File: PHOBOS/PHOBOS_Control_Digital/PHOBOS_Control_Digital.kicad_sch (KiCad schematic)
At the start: 79 parts, among them J1 Conn_01x06, J12 PWR, J14 PS1-2, J15 PS3-4, J2 RF_OUT, J3 USB4056-03-A_REVA2, J4 Screw_Terminal_01x02, J8 Conn_01x02, SW1 KMR211GLFS, U1 SX1280IMLTRT, U2 W25Q128JVSIQ, U3 NCP1117-3.3_SOT223, U4 RP2040, U5 TPS60403DBV, Y1 C1E-52.000-10-1012-X-M, Y2 ABM8-272-T3

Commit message: Schematic cleaned up for review.
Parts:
- removed J1: Conn_01x06, Connector_PinHeader_2.54mm:PinHeader_1x06_P2.54mm_Vertical, symbol Connector_Generic:Conn_01x06
- removed R2: 10k, Resistor_SMD:R_0402_1005Metric, symbol Device:R
- removed SW1: KMR211GLFS, External/Custom Parts:KMR2xxG_CNK, symbol KMR2xxG_CNK:KMR211GLFS
- removed TP12: GPIO22, TestPoint:TestPoint_THTPad_D2.0mm_Drill1.0mm, symbol Connector:TestPoint
- removed TP3: SCK_TRANS, TestPoint:TestPoint_Plated_Hole_D2.0mm, symbol Connector:TestPoint
- removed TP4: MOSI_TRANS, TestPoint:TestPoint_Plated_Hole_D2.0mm, symbol Connector:TestPoint
- removed TP5: MISO_TRANS, TestPoint:TestPoint_Plated_Hole_D2.0mm, symbol Connector:TestPoint
- removed TP6: CS, TestPoint:TestPoint_Plated_Hole_D2.0mm, symbol Connector:TestPoint
- J8: value Conn_01x02 -> BOOT; now left out of the parts list
- TP11: value GPIO22 -> GPIO19
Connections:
- net RUN: no longer names the net of U4.26 (RUN)
- no-connect marks 22 -> 25
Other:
- note added: "-3V Charge Pump"
- note added: "Connectors"
- note added: "Transceiver"
- note removed: "Boot Select"
- note removed: "Exclude From Board"
- note removed: "Filtering"
- note removed: "Make sure C10 is close to pin 44 of RP2040 ***C10 is out of date. figure out***"
- note removed: "Make sure R3 and R4 are close to RP2040"
- note removed: "Reset"
- note removed: "SPI1"
- moved on the sheet: C0, C1, C10, C11, C12, C13, C14, C15, C16, C17, C2, C3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

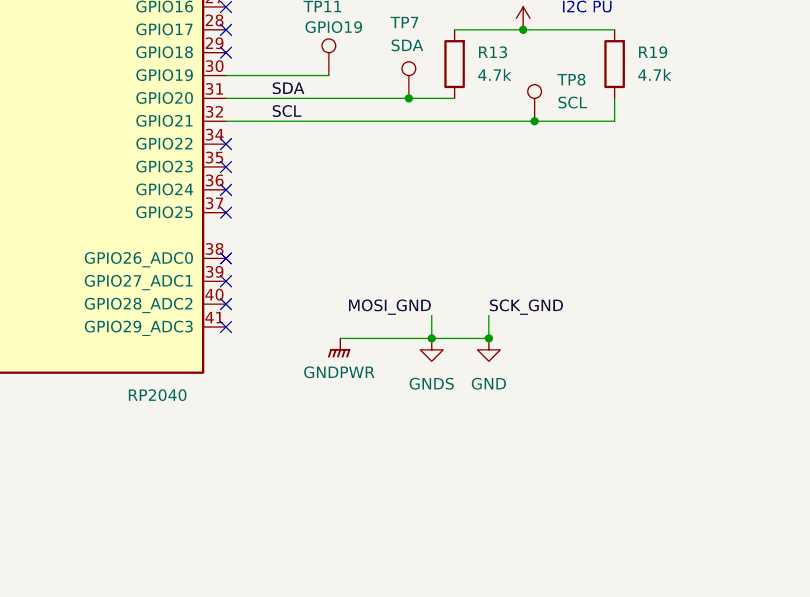
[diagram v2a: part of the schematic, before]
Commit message: Batt measure added
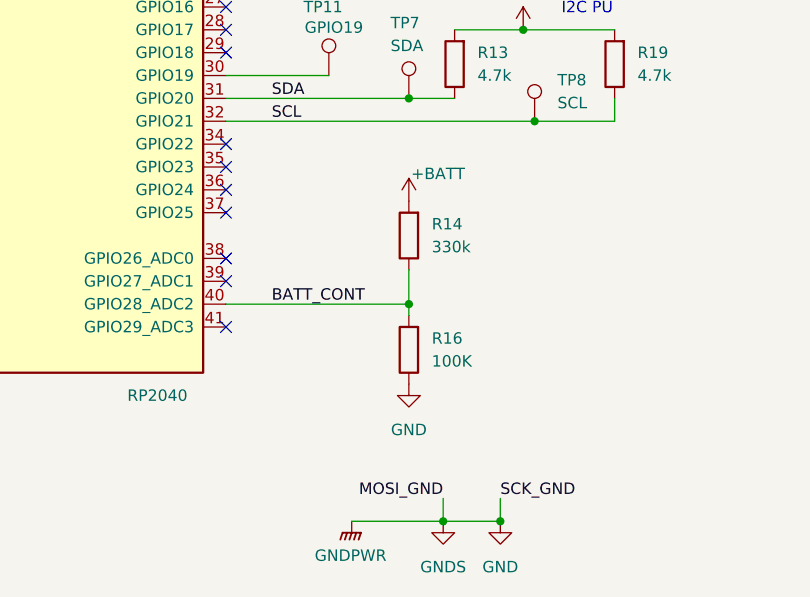
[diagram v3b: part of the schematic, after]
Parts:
- added R14: 330k, Resistor_SMD:R_0402_1005Metric, symbol Device:R
- added R16: 100K, Resistor_SMD:R_0402_1005Metric, symbol Device:R
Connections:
- net +BATT: now also R14.2
- net GND: now also R16.1
- net BATT_CONT: now reaches U4.40 (GPIO28_ADC2)
- net BATT_CONT: now also R14.1, R16.2
- no-connect marks 25 -> 24
